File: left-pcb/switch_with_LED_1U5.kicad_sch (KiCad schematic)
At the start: 3 parts, among them SW1 SW_SPST

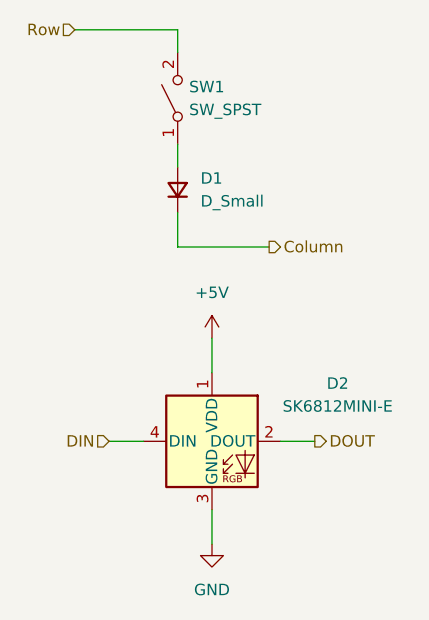
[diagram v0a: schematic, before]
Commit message: Updating schematic with different size keys
Also updated LED data wiring to correspond with PCB layout
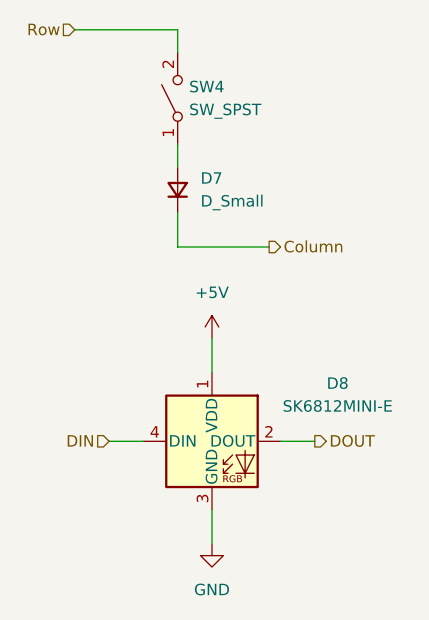
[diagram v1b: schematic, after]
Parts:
- SW4: renamed from SW1; footprint PCM_Switch_Keyboard_Hotswap_Kailh:SW_Hotswap_Kailh_MX_1.00u -> PCM_Switch_Keyboard_Hotswap_Kailh:SW_Hotswap_Kailh_MX_1.50u
- renumbered D1 to D7, D2 to D8
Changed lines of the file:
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@@
 		(dnp no)
 		(fields_autoplaced yes)
-		(property "Reference" "D2"
+		(property "Reference" "D8"
 			(at 138.43 125.6598 0)
 			(effects
@@
 		(dnp no)
 		(fields_autoplaced yes)
-		(property "Reference" "#PWR011"
+		(property "Reference" "#PWR017"
 			(at 124.46 149.86 0)
 			(effects
@@
 		(dnp no)
 		(fields_autoplaced yes)
-		(property "Reference" "SW1"
+		(property "Reference" "SW4"
 			(at 121.92 92.7099 90)
 			(effects
@@
 			)
 		)
-		(property "Footprint" "PCM_Switch_Keyboard_Hotswap_Kailh:SW_Hotswap_Kailh_MX_1.00u"
+		(property "Footprint" "PCM_Switch_Keyboard_Hotswap_Kailh:SW_Hotswap_Kailh_MX_1.50u"
 			(at 120.65 93.98 0)
 			(effects
@@
 		(dnp no)
 		(fields_autoplaced yes)
-		(property "Reference" "D1"
+		(property "Reference" "D7"
 			(at 123.19 102.8699 90)
 			(effects
@@
 		(dnp no)
 		(fields_autoplaced yes)
-		(property "Reference" "#PWR010"
+		(property "Reference" "#PWR016"
 			(at 124.46 124.46 0)
 			(effects

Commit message: Initial modifications to reduce fab cost and add caps
Removing 1 row and column of keys, and majorly changing layout

Routing still in progress
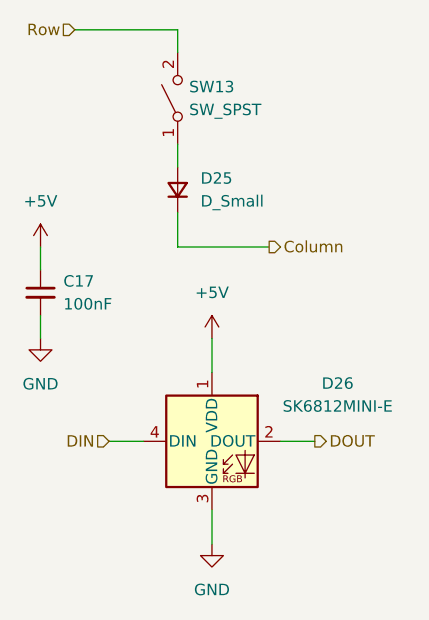
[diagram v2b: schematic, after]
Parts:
- removed D7: D_Small, Diode_SMD:D_SOD-123, symbol Device:D_Small
- removed D8: SK6812MINI-E, SW-Adafruit:LED_SK6812MINI-E_REVERSE_MOUNT_3.2x2.8mm_P1.09mm, symbol SW-Adafruit:SK6812MINI-E
- removed SW4: SW_SPST, PCM_Switch_Keyboard_Hotswap_Kailh:SW_Hotswap_Kailh_MX_1.50u, symbol Switch:SW_SPST
- added C17: 100nF, Capacitor_SMD:C_1206_3216Metric_Pad1.33x1.80mm_HandSolder, symbol Device:C_Small
- added D25: D_Small, Diode_SMD:D_SOD-123, symbol Device:D_Small
- added D26: SK6812MINI-E, SW-Adafruit:LED_SK6812MINI-E_REVERSE_MOUNT_3.2x2.8mm_P1.09mm, symbol SW-Adafruit:SK6812MINI-E
- added SW13: SW_SPST, PCM_Switch_Keyboard_Hotswap_Kailh:SW_Hotswap_Kailh_MX_1.50u, symbol Switch:SW_SPST
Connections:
- net +5V: now also C17.1, D26.1 (VDD)
- net Column: now also D25.1 (K)
- net DIN: now also D26.4 (DIN)
- net DOUT: now also D26.2 (DOUT)
- net GND: now also C17.2, D26.3 (GND)
- net Row: now also SW13.2 (B)
- new net: D25.2 (A), SW13.1 (A)

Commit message: Caps, shrunk board, added mounting holes
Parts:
- C17: footprint Capacitor_SMD:C_1206_3216Metric_Pad1.33x1.80mm_HandSolder -> Capacitor_SMD:C_0805_2012Metric_Pad1.18x1.45mm_HandSolder
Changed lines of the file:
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@@
 			)
 		)
-		(property "Footprint" "Capacitor_SMD:C_1206_3216Metric_Pad1.33x1.80mm_HandSolder"
+		(property "Footprint" "Capacitor_SMD:C_0805_2012Metric_Pad1.18x1.45mm_HandSolder"
 			(at 105.41 115.57 0)
 			(effects

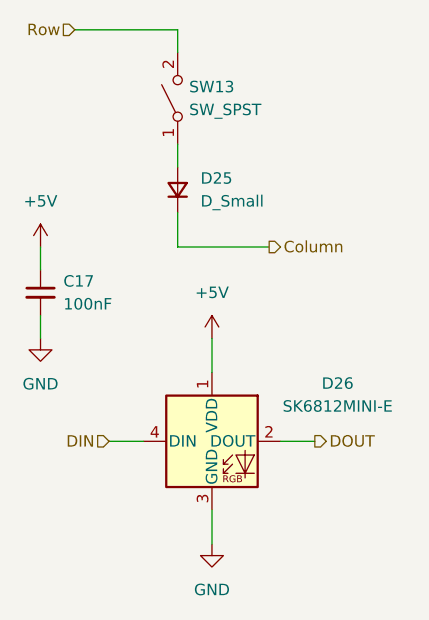
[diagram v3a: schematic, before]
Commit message: Adding values to Diodes and adding stabilizers to 2U switches
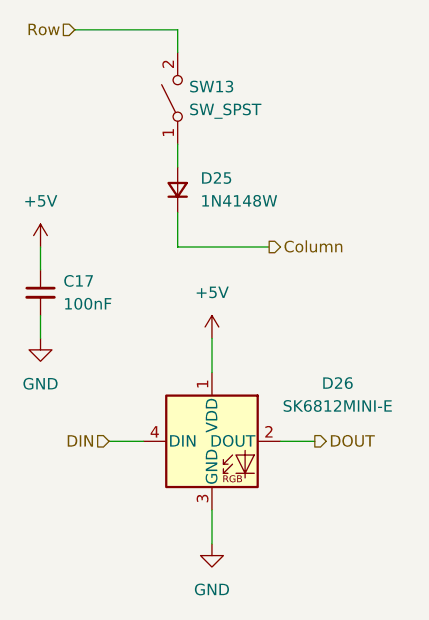
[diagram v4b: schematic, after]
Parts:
- D25: value D_Small -> 1N4148W
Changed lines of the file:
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@@
 			)
 		)
-		(property "Value" "D_Small"
+		(property "Value" "1N4148W"
 			(at 123.19 105.4099 90)
 			(effects

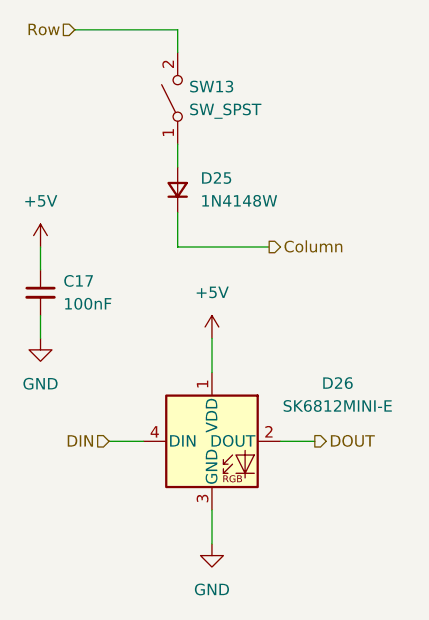
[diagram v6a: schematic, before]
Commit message: adding mounting hole in center for additional support, and cleaning up tracks/zones
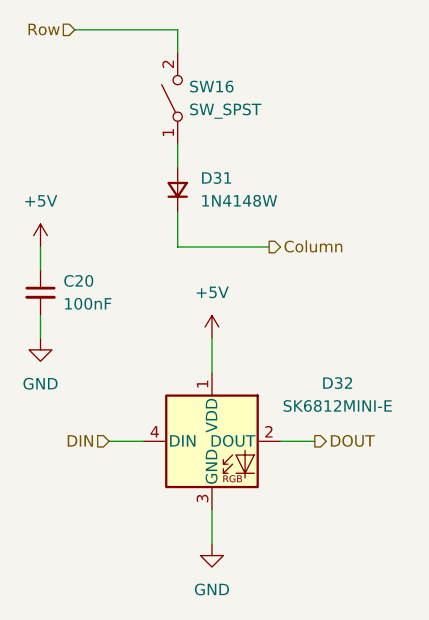
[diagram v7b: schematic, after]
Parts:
- renumbered C17 to C20, D25 to D31, D26 to D32, SW13 to SW16
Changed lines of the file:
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@@
+	(wire
+		(pts
+			(xy 120.65 106.68) (xy 120.65 110.49)
+		)
+		(stroke
+			(width 0)
+			(type default)
+		)
+	)
 	(wire
 		(pts
@@
 	(wire
 		(pts
+			(xy 109.22 86.36) (xy 120.65 86.36)
+		)
+		(stroke
+			(width 0)
+			(type default)
+		)
+	)
+	(wire
+		(pts
+			(xy 124.46 139.7) (xy 124.46 143.51)
+		)
+		(stroke
+			(width 0)
+			(type default)
+		)
+	)
+	(wire
+		(pts
+			(xy 105.41 118.11) (xy 105.41 120.65)
+		)
+		(stroke
+			(width 0)
+			(type default)
+		)
+	)
+	(wire
+		(pts
+			(xy 132.08 132.08) (xy 135.89 132.08)
+		)
+		(stroke
+			(width 0)
+			(type default)
+		)
+	)
+	(wire
+		(pts
 			(xy 120.65 99.06) (xy 120.65 101.6)
 		)
@@
 	(wire
 		(pts
-			(xy 132.08 132.08) (xy 135.89 132.08)
-		)
-		(stroke
-			(width 0)
-			(type default)
-		)
-	)
-	(wire
-		(pts
-			(xy 109.22 86.36) (xy 120.65 86.36)
-		)
-		(stroke
-			(width 0)
-			(type default)
-		)
-	)
-	(wire
-		(pts
-			(xy 105.41 118.11) (xy 105.41 120.65)
+			(xy 124.46 120.65) (xy 124.46 124.46)
 		)
 		(stroke
@@
 	(wire
 		(pts
-			(xy 124.46 139.7) (xy 124.46 143.51)
-		)
-		(stroke
-			(width 0)
-			(type default)
-		)
-	)
-	(wire
-		(pts
-			(xy 124.46 120.65) (xy 124.46 124.46)
-		)
-		(stroke
-			(width 0)
-			(type default)
-		)
-	)
-	(wire
-		(pts
 			(xy 105.41 110.49) (xy 105.41 113.03)
-		)
-		(stroke
-			(width 0)
-			(type default)
-		)
-	)
-	(wire
-		(pts
-			(xy 120.65 106.68) (xy 120.65 110.49)
 		)
 		(stroke
@@
 		(dnp no)
 		(fields_autoplaced yes)
-		(property "Reference" "D25"
+		(property "Reference" "D31"
 			(at 123.19 102.8699 90)
 			(show_name no)
@@
 			(project "row_staggered_split_keyboard_left_side"
 				(path "/cf145565-22e2-4e5a-8a27-915862c57a1b/57cf96a1-6bb7-4988-8767-6c5d987c352c"
-					(reference "D25")
+					(reference "D31")
 					(unit 1)
 				)
@@
 		(dnp no)
 		(fields_autoplaced yes)
-		(property "Reference" "C17"
+		(property "Reference" "C20"
 			(at 107.95 114.3062 0)
 			(show_name no)
@@
 			(project "row_staggered_split_keyboard_left_side"
 				(path "/cf145565-22e2-4e5a-8a27-915862c57a1b/57cf96a1-6bb7-4988-8767-6c5d987c352c"
-					(reference "C17")
+					(reference "C20")
 					(unit 1)
 				)
@@
 		(dnp no)
 		(fields_autoplaced yes)
-		(property "Reference" "#PWR068"
+		(property "Reference" "#PWR080"
 			(at 124.46 149.86 0)
 			(hide yes)
@@
 			(project "row_staggered_split_keyboard_left_side"
 				(path "/cf145565-22e2-4e5a-8a27-915862c57a1b/57cf96a1-6bb7-4988-8767-6c5d987c352c"
-					(reference "#PWR068")
+					(reference "#PWR080")
 					(unit 1)
 				)
@@
 		(dnp no)
 		(fields_autoplaced yes)
-		(property "Reference" "SW13"
+		(property "Reference" "SW16"
 			(at 121.92 92.7099 90)
 			(show_name no)
@@
 			(project "row_staggered_split_keyboard_left_side"
 				(path "/cf145565-22e2-4e5a-8a27-915862c57a1b/57cf96a1-6bb7-4988-8767-6c5d987c352c"
-					(reference "SW13")
+					(reference "SW16")
 					(unit 1)
 				)
@@
 		(dnp no)
 		(fields_autoplaced yes)
-		(property "Reference" "D26"
+		(property "Reference" "D32"
 			(at 138.43 125.6598 0)
 			(show_name no)
@@
 			(project "row_staggered_split_keyboard_left_side"
 				(path "/cf145565-22e2-4e5a-8a27-915862c57a1b/57cf96a1-6bb7-4988-8767-6c5d987c352c"
-					(reference "D26")
+					(reference "D32")
 					(unit 1)
 				)
@@
 		(dnp no)
 		(fields_autoplaced yes)
-		(property "Reference" "#PWR065"
+		(property "Reference" "#PWR077"
 			(at 105.41 114.3 0)
 			(hide yes)
@@
 			(project "row_staggered_split_keyboard_left_side"
 				(path "/cf145565-22e2-4e5a-8a27-915862c57a1b/57cf96a1-6bb7-4988-8767-6c5d987c352c"
-					(reference "#PWR065")
+					(reference "#PWR077")
 					(unit 1)
 				)
@@
 		(dnp no)
 		(fields_autoplaced yes)
-		(property "Reference" "#PWR067"
+		(property "Reference" "#PWR079"
 			(at 124.46 124.46 0)
 			(hide yes)
@@
 			(project "row_staggered_split_keyboard_left_side"
 				(path "/cf145565-22e2-4e5a-8a27-915862c57a1b/57cf96a1-6bb7-4988-8767-6c5d987c352c"
-					(reference "#PWR067")
+					(reference "#PWR079")
 					(unit 1)
 				)
@@
 		(dnp no)
 		(fields_autoplaced yes)
-		(property "Reference" "#PWR066"
+		(property "Reference" "#PWR078"
 			(at 105.41 127 0)
 			(hide yes)
@@
 			(project "row_staggered_split_keyboard_left_side"
 				(path "/cf145565-22e2-4e5a-8a27-915862c57a1b/57cf96a1-6bb7-4988-8767-6c5d987c352c"
-					(reference "#PWR066")
+					(reference "#PWR078")
 					(unit 1)
 				)

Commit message: Boards were ordered
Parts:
- SW16: symbol Switch:SW_SPST -> SW-gElectroMech:SPST_MOM
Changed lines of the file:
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@@
 	)
 	(symbol
-		(lib_id "Switch:SW_SPST")
+		(lib_id "SW-gElectroMech:SPST_MOM")
 		(at 120.65 93.98 90)
 		(unit 1)
@@
 		)
 		(property "Datasheet" ""
-			(at 120.65 93.98 0)
+			(at 115.57 93.98 0)
 			(hide yes)
 			(show_name no)
@@
 			)
 		)
-		(property "Description" "Single Pole Single Throw (SPST) switch"
+		(property "Description" "Push button switch, generic, two pins"
 			(at 120.65 93.98 0)
 			(hide yes)
